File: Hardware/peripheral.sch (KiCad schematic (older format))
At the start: 77 parts, among them J1 UFL, Q1 MMBT4403, U1 PCF8563T, U2 HX711, U3 TPL5110, U4 MB85RC16PNF-G-JNE1, U5 RFM95W-868S2, U6 W25Q32JVSS, U7 24LC02B_SN, Y1 Crystal_Small

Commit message: Add pcb route and ground plane
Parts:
- removed Q1: MMBT4403, symbol EcoApi_pcb:MMBT4403
- removed R12, R13: 0R, Resistor_SMD:R_0603_1608Metric, symbol Device:R
- removed TP1, TP10, TP11, TP12, TP13, TP14, TP15, TP16, TP17, TP18, TP2, TP3, TP5, TP6, TP7, TP8, TP9: TestPoint, TestPoint:TestPoint_Pad_D1.5mm, symbol Connector:TestPoint
- removed U1: PCF8563T, Package_SO:SOIC-8_3.9x4.9mm_P1.27mm, symbol Timer_RTC:PCF8563T
- removed U3: TPL5110, Package_TO_SOT_SMD:SOT-23-6, symbol Timer:TPL5110
- added C25: 10uF, Capacitor_SMD:C_0603_1608Metric, symbol Device:C
- added IC1: PCF8563T_5,518, EcoApi_pcb:SOIC127P600X175-8N, symbol EcoApi_pcb:PCF8563T_5,518
- added Q1: MMBT4403*, EcoApi_pcb:SOT23-BEC, symbol EcoApi_pcb:MMBT4403*
- added U1: TPL5010DDCR, EcoApi_pcb:SOT95P280X110-6N, symbol EcoApi_pcb:TPL5010DDCR
- C1: value 10uF -> 22pF; footprint Capacitor_SMD:C_0603_1608Metric -> Capacitor_SMD:C_0201_0603Metric
- C3: footprint Capacitor_SMD:C_0603_1608Metric -> Capacitor_SMD:C_0201_0603Metric
- L1: value 3.3uH -> 3.3uH_0603; footprint (none) -> Inductor_SMD:L_0603_1608Metric_Pad1.05x0.95mm_HandSolder
- R4: value 100R 0805 -> 100R
- TP4: footprint TestPoint:TestPoint_Pad_D1.5mm -> TestPoint:TestPoint_Pad_D1.0mm
- U2: footprint (none) -> EcoApi_pcb:Avia_Semiconductor-HX711-IPC_A
- U6: footprint Package_SO:SOIC-8_5.23x5.23mm_P1.27mm -> EcoApi_pcb:SOIC127P790X216-8N
- Y1: footprint (none) -> EcoApi_pcb:XTAL_ABS07-120-32.768KHZ-T
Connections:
- net labels removed: LOADCELL_E-, LOADCELL_SHIELD, LORA_DIO3
- wire segments 217 -> 210
- no-connect marks 6 -> 7
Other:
- note removed: "ana ground ???"
- moved on the sheet: C2, R1, R14, R15, R16, R17, R2, R3, R6, R9

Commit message: Fix drc error
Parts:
- added R58: 10K, Resistor_SMD:R_0603_1608Metric, symbol Device:R
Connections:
- net WDG_ALARM: now also R58.1
- net at C2.1, R14.2, R15.2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: now also R58.2
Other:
- note removed: "nrst !!! if rtc not mount"
- moved on the sheet: R16
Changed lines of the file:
@@
 Text Notes 8500 6400 0    50   ~ 0
 Serie protection resistor ?
-Text Notes 1800 2650 0    50   ~ 0
-nrst !!! if rtc not mount
 Text Notes -2000 4250 0    50   ~ 0
 32.768kHz (smd3215-2p)\nfor pcf8563x (ESR 100K, Load C 12.5pF, C trim 5-25pf)\nSC-32S32.768kHz20PPM12.5pF\n\nfor DS1337C, DS1339C (ESR 50K, Load C 6pF)\nSC-32S32.768kHz20PPM6pF\n\nfor DS1372U (ESR  50K, Load C 12.5pF)\nSC-32S32.768kHz20PPM12.5pF\n\n
@@
 $EndComp
 $Comp
-L Device:R R?
-U 1 1 637DE7C1
-P 1600 2000
-AR Path="/637DE7C1" Ref="R?"  Part="1"
-AR Path="/62D38F6A/637DE7C1" Ref="R?"  Part="1"
-AR Path="/62EA3721/637DE7C1" Ref="R16"  Part="1"
-F 0 "R16" H 1670 2046 50  0000 L CNN
-F 1 "10K" H 1670 1955 50  0000 L CNN
-F 2 "Resistor_SMD:R_0603_1608Metric" V 1530 2000 50  0001 C CNN
-F 3 "~" H 1600 2000 50  0001 C CNN
-	1    1600 2000
-	1    0    0    -1
-$EndComp
-$Comp
 L power:GND #PWR?
 U 1 1 637E960E
-P 1600 2450
+P 1050 2450
 AR Path="/637E960E" Ref="#PWR?"  Part="1"
 AR Path="/62D38F6A/637E960E" Ref="#PWR?"  Part="1"
 AR Path="/62EA3721/637E960E" Ref="#PWR0165"  Part="1"
-F 0 "#PWR0165" H 1600 2200 50  0001 C CNN
-F 1 "GND" H 1605 2277 50  0000 C CNN
-F 2 "" H 1600 2450 50  0001 C CNN
-F 3 "" H 1600 2450 50  0001 C CNN
-	1    1600 2450
+F 0 "#PWR0165" H 1050 2200 50  0001 C CNN
+F 1 "GND" H 1055 2277 50  0000 C CNN
+F 2 "" H 1050 2450 50  0001 C CNN
+F 3 "" H 1050 2450 50  0001 C CNN
+	1    1050 2450
 	1    0    0    -1
 $EndComp
@@
 	3050 4150 3050 4200
 Wire Wire Line
-	3500 1350 3900 1350
+	3500 1350 3650 1350
 Wire Wire Line
 	3900 1100 3900 1200
@@
 	3900 2350 3500 2350
 Connection ~ 3900 2350
-Text GLabel 1900 2000 3    50   Output ~ 0
+Text GLabel 1700 2350 0    50   Output ~ 0
 WDG_ALARM
 Wire Wire Line
@@
 	2050 650  2050 850
 Connection ~ 2050 850
-Wire Wire Line
-	1600 2150 1600 2450
-Wire Wire Line
-	1600 1850 1600 1750
 Connection ~ 1600 1750
 Wire Wire Line
@@
 Wire Wire Line
 	2100 1950 1900 1950
-Wire Wire Line
-	1900 1950 1900 2000
 NoConn ~ 2100 2150
 Wire Wire Line
@@
 	1    0    0    -1
 $EndComp
+Wire Wire Line
+	1600 1750 1600 1950
+Wire Wire Line
+	1200 1950 1050 1950
+Wire Wire Line
+	1050 1950 1050 2450
+Wire Wire Line
+	1700 2350 1900 2350
+Wire Wire Line
+	1900 1950 1900 2350
+Connection ~ 1900 2350
+Connection ~ 3650 1350
+Wire Wire Line
+	3650 1350 3900 1350
+Wire Wire Line
+	1600 1950 1500 1950
+$Comp
+L Device:R R?
+U 1 1 637DE7C1
+P 1350 1950
+AR Path="/637DE7C1" Ref="R?"  Part="1"
+AR Path="/62D38F6A/637DE7C1" Ref="R?"  Part="1"
+AR Path="/62EA3721/637DE7C1" Ref="R16"  Part="1"
+F 0 "R16" H 1420 1996 50  0000 L CNN
+F 1 "10K" H 1420 1905 50  0000 L CNN
+F 2 "Resistor_SMD:R_0603_1608Metric" V 1280 1950 50  0001 C CNN
+F 3 "~" H 1350 1950 50  0001 C CNN
+	1    1350 1950
+	0    1    1    0
+$EndComp
+$Comp
+L Device:R R?
+U 1 1 620F7DE3
+P 2100 2650
+AR Path="/620F7DE3" Ref="R?"  Part="1"
+AR Path="/62D38F6A/620F7DE3" Ref="R?"  Part="1"
+AR Path="/62EA3721/620F7DE3" Ref="R58"  Part="1"
+F 0 "R58" H 2170 2696 50  0000 L CNN
+F 1 "10K" H 2170 2605 50  0000 L CNN
+F 2 "Resistor_SMD:R_0603_1608Metric" V 2030 2650 50  0001 C CNN
+F 3 "~" H 2100 2650 50  0001 C CNN
+	1    2100 2650
+	0    -1   -1   0
+$EndComp
+Wire Wire Line
+	1900 2650 1950 2650
+Wire Wire Line
+	1900 2350 1900 2650
+Wire Wire Line
+	2250 2650 3650 2650
+Wire Wire Line
+	3650 1350 3650 2650
 $EndSCHEMATC

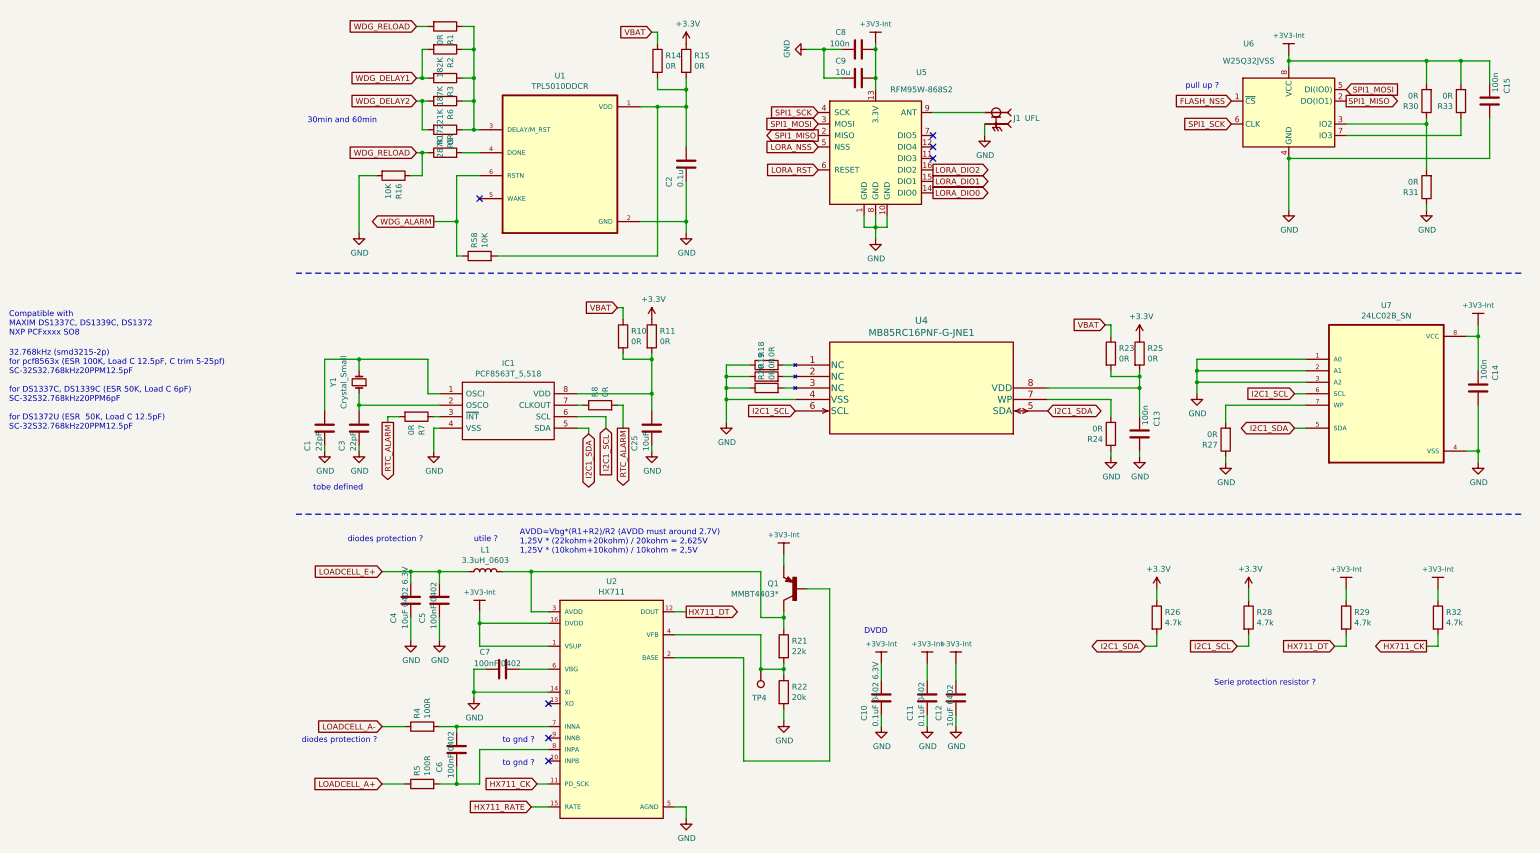
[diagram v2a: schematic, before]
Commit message: Update pcb to v2.1 (Add ldo)
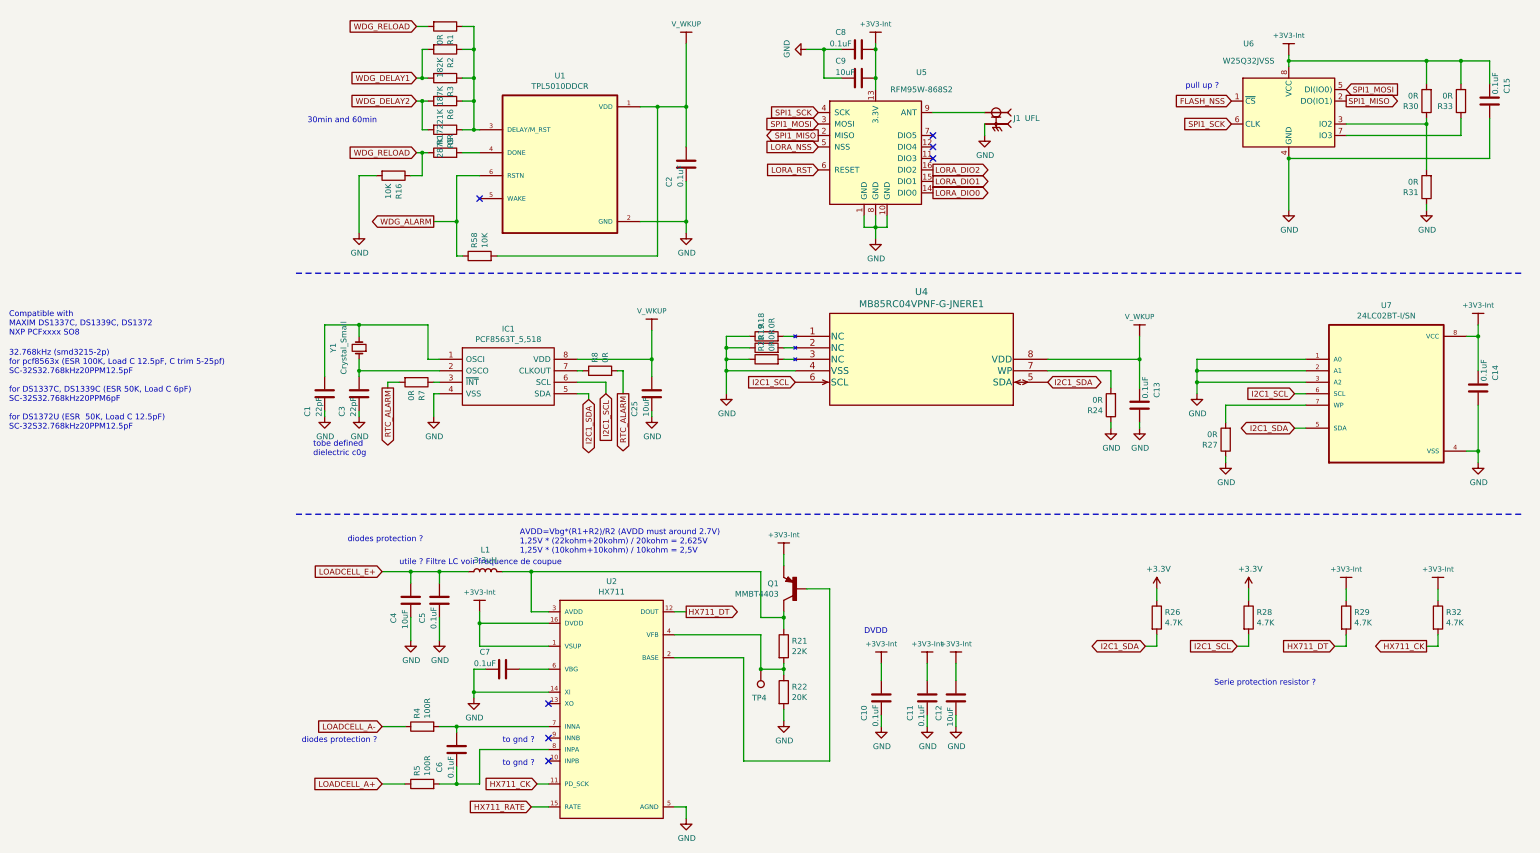
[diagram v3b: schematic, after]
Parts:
- removed R10, R11, R14, R15, R23, R25: 0R, Resistor_SMD:R_0603_1608Metric, symbol Device:R
- C1, C3: Populate (none) -> yes; Size Inch (none) -> 0201; Size Metric (none) -> 0603
- C10: value 0.1uF 0402 6.3V -> 0.1uF; Populate (none) -> yes; Size Inch (none) -> 0603; Size Metric (none) -> 1608; Voltage (none) -> 6.3V
- C11: value 0.1uF 0402 -> 0.1uF; Populate (none) -> yes; Size Inch (none) -> 0603; Size Metric (none) -> 1608
- C12: value 10uF 0402 -> 10uF; Populate (none) -> yes; Size Inch (none) -> 0603; Size Metric (none) -> 1608
- C13, C14, C15, C8: value 100n -> 0.1uF; Populate (none) -> yes; Size Inch (none) -> 0603; Size Metric (none) -> 1608
- C2, C25: Populate (none) -> yes; Size Inch (none) -> 0603; Size Metric (none) -> 1608
- C4: value 10uF 0402 6.3V -> 10uF; Populate (none) -> yes; Size Inch (none) -> 0603; Size Metric (none) -> 1608; Voltage (none) -> 6.3V
- C5, C6, C7: value 100nF 0402 -> 0.1uF; Populate (none) -> yes; Size Inch (none) -> 0603; Size Metric (none) -> 1608
- C9: value 10u -> 10uF; Populate (none) -> yes; Size Inch (none) -> 0603; Size Metric (none) -> 1608
- IC1: Populate (none) -> yes; package (none) -> SOIC-8
- J1, U5: Populate (none) -> no
- L1: value 3.3uH_0603 -> 3.3uH; Populate (none) -> yes; Size Inch (none) -> 0603; Size Metric (none) -> 1608
- Q1: value MMBT4403* -> MMBT4403; Manufacturer_Part_Number (none) -> MMBT4403; Populate (none) -> yes; package (none) -> SOT-23-3
- R1, R16, R17, R2, R24, R27, R3, R4, R5, R58, R6, R7, R9: Populate (none) -> yes; Size Inch (none) -> 0603; Size Metric (none) -> 1608; Tolerance (none) -> 1%
- R18, R19, R20, R8: Populate (none) -> no; Size Inch (none) -> 0603; Size Metric (none) -> 1608; Tolerance (none) -> 1%
- R21: value 22k -> 22K; Populate (none) -> yes; Size Inch (none) -> 0603; Size Metric (none) -> 1608; Tolerance (none) -> 1%
- R22: value 20k -> 20K; Populate (none) -> yes; Size Inch (none) -> 0603; Size Metric (none) -> 1608; Tolerance (none) -> 1%
- R26, R28, R29, R32: value 4.7k -> 4.7K; Populate (none) -> yes; Size Inch (none) -> 0603; Size Metric (none) -> 1608; Tolerance (none) -> 1%
- R30, R31, R33: Size Inch (none) -> 0603; Size Metric (none) -> 1608; Tolerance (none) -> 1%
- TP4, U2, Y1: Populate (none) -> yes
- U1: Manufacturer_Name (none) -> Texas Instruments; Manufacturer_Part_Number (none) -> TPL5010DDCR; Populate (none) -> yes; package (none) -> SOT-23-6
- U4: value MB85RC16PNF-G-JNE1 -> MB85RC04VPNF-G-JNERE1; Manufacturer_Name (none) -> Fujitsu Semiconductor; Manufacturer_Part_Number (none) -> MB85RC04VPNF-G-JNERE1; Populate (none) -> yes; package (none) -> SOP-8
- U6: Manufacturer_Name (none) -> Winbond; Manufacturer_Part_Number (none) -> W25Q32JVSSIQ; Populate (none) -> yes; package (none) -> SOIC-8
- U7: value 24LC02B_SN -> 24LC02BT-I/SN; Manufacturer_Name (none) -> Microchip; Manufacturer_Part_Number (none) -> 24LC02BT-I/SN; Populate (none) -> yes; package (none) -> SOIC-8
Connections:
- net V_WKUP: now reaches C2.1, R58.2, U1.1 (VDD)
- net V_WKUP: now also C13.2, C25.1, IC1.8 (VDD), U4.8 (VDD)
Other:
- note added: "tobe defined \ndielectric c0g"
- note added: "utile ? Filtre LC voir frequence de coupue"
- note removed: "tobe defined"
- note removed: "utile ?"
- moved on the sheet: C1, C13, C25, C3, IC1, R18, R19, R20, R24, R7, R8, U4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
